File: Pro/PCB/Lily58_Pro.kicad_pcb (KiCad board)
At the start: 2 copper layers, 142.5 x 106.3 mm, 87 parts, among them J1 LED, J2 4PIN, J3 OLED, P1 i2c_pin, P2 i2c_pin, SW1 SW_PUSH, SW10 SW_PUSH, SW11 SW_PUSH, SW12 SW_PUSH, SW13 SW_PUSH, SW14 SW_PUSH, SW15 SW_PUSH, SW16 SW_PUSH, SW17 SW_PUSH, SW18 SW_PUSH, SW19 SW_PUSH, SW2 SW_PUSH, SW20 SW_PUSH, SW21 SW_PUSH, SW22 SW_PUSH, SW23 SW_PUSH, SW24 SW_PUSH, SW25 SW_PUSH, SW26 SW_PUSH, SW27 SW_PUSH, SW28 SW_PUSH, SW29 SW_PUSH, SW3 SW_PUSH, SW4 SW_PUSH, SW5 SW_PUSH, SW6 SW_PUSH, SW7 SW_PUSH, SW8 SW_PUSH, SW9 SW_PUSH, U1 ProMicro

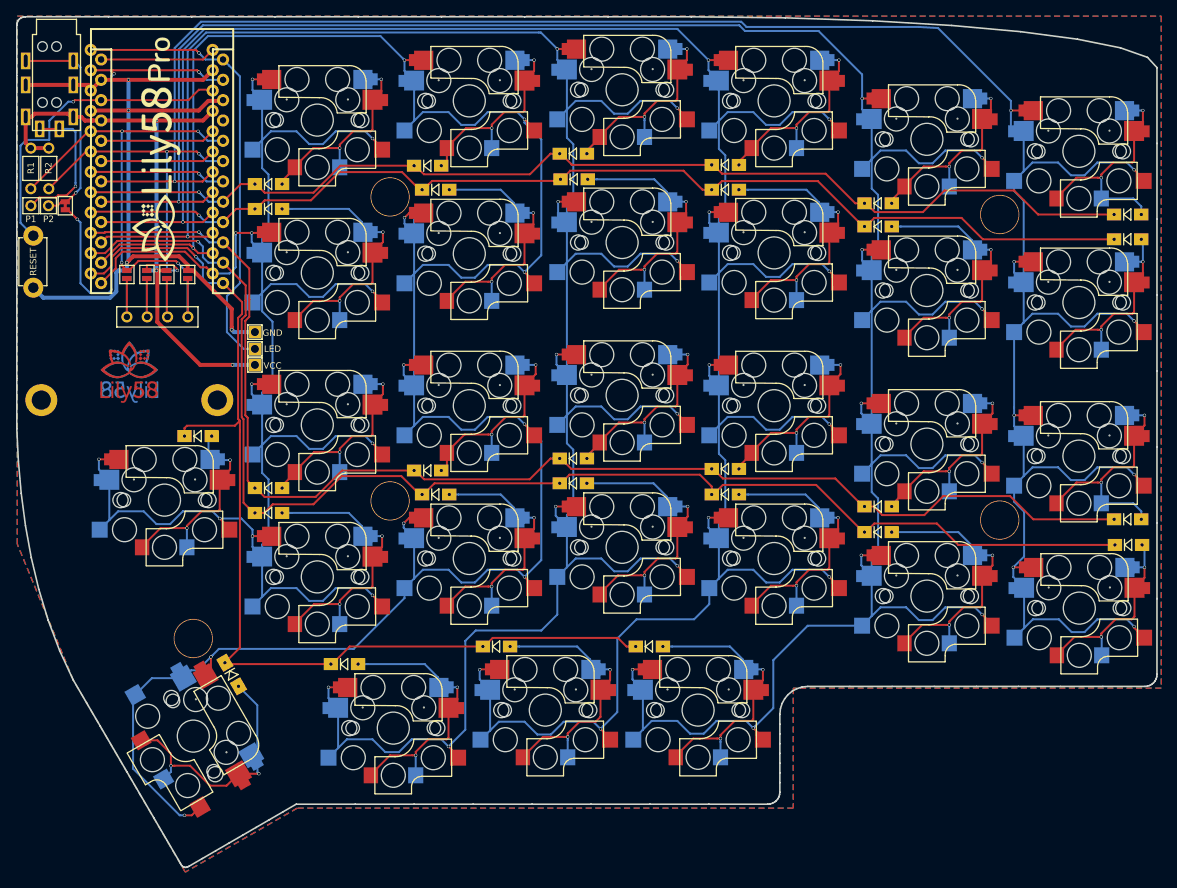
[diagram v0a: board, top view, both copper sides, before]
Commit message: Fixed gaps in copper fills
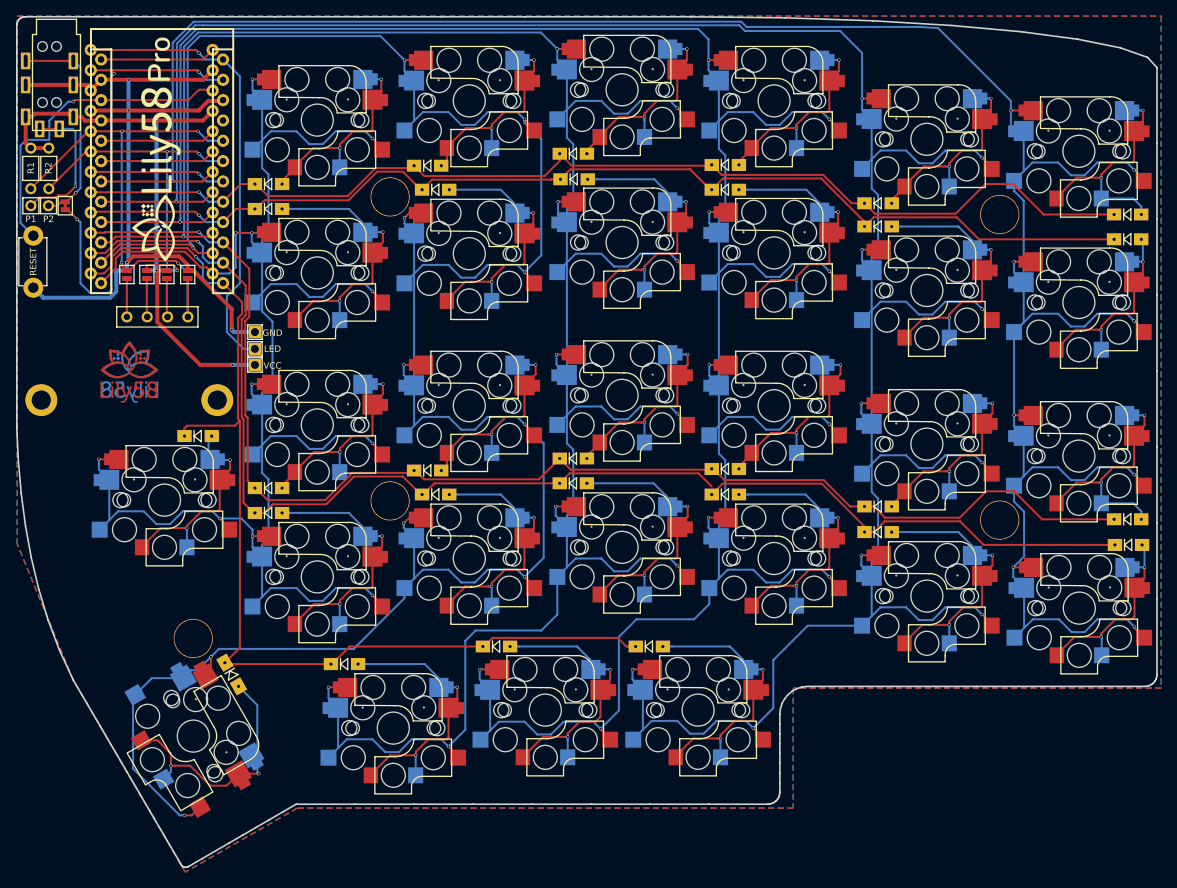
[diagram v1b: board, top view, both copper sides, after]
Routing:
- net col1: track 350.6 -> 352.9 mm
- net col2: track 334.4 -> 336.7 mm
- net row0: track 138.2 -> 140.1 mm
- net col4: track 319.5 -> 320.9 mm
- net row2: track 165.8 -> 166.9 mm
- net row1: track 138.3 -> 139.1 mm
- net col3: track 319.9 -> 320.6 mm
- net col0: track 304.4 -> 305.0 mm
